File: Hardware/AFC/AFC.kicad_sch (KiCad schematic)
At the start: 80 parts, among them J1 Barrel_Jack_Switch, J2 Conn_Coaxial, J3 Conn_Coaxial, J4 Conn_Coaxial, J5 Conn_Coaxial, J6 Conn_Coaxial, J7 Conn_Coaxial, U1 AD633JRZ, U2 AD633JRZ, U3 AD630ARZ, U4 AD8429, U5 AD8429, U6 LM358, U7 LM358, U8 LM358

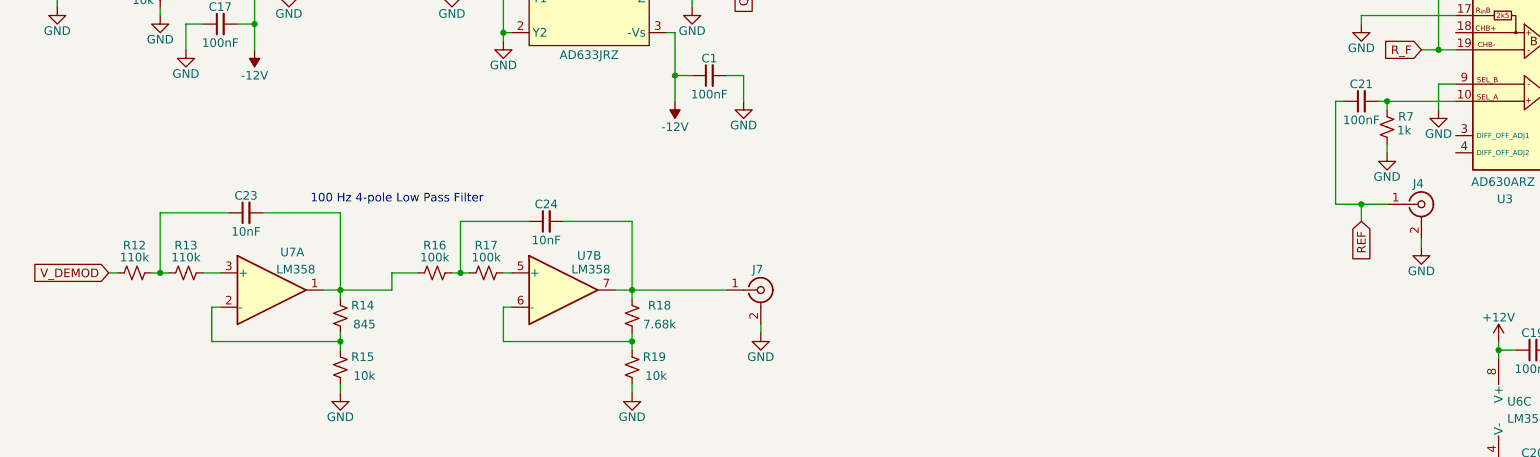
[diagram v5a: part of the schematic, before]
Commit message: Updating resistor values in filter
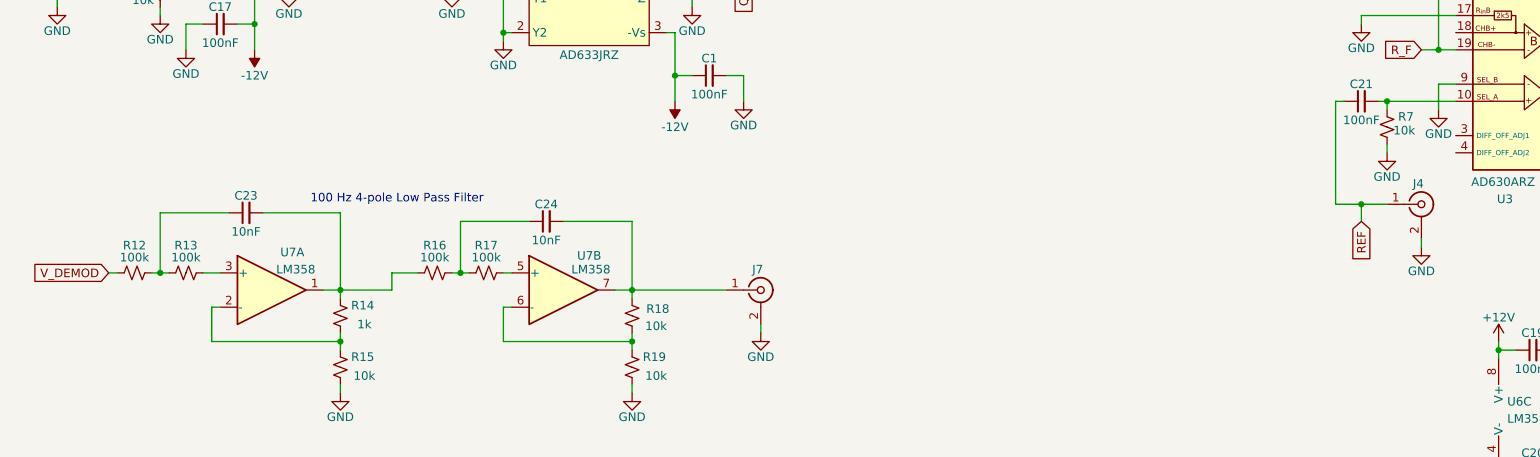
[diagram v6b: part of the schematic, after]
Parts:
- R12, R13: value 110k -> 100k
- R14: value 845 -> 1k
- R18: value 7.68k -> 10k
- R7: value 1k -> 10k
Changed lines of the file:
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@@
 			)
 		)
-		(property "Value" "110k"
+		(property "Value" "100k"
 			(at 34.29 125.984 90)
 			(effects
@@
 			)
 		)
-		(property "Value" "110k"
+		(property "Value" "100k"
 			(at 41.91 125.984 90)
 			(effects
@@
 		(dnp no)
 		(property "Reference" "R18"
-			(at 112.014 133.096 0)
+			(at 111.76 133.604 0)
 			(effects
 				(font
@@
 			)
 		)
-		(property "Value" "7.68k"
-			(at 112.014 135.89 0)
+		(property "Value" "10k"
+			(at 111.506 136.144 0)
 			(effects
 				(font
@@
 			)
 		)
-		(property "Value" "845"
+		(property "Value" "1k"
 			(at 68.326 135.89 0)
 			(effects
@@
 			)
 		)
-		(property "Value" "1k"
+		(property "Value" "10k"
 			(at 222.25 107.188 0)
 			(effects

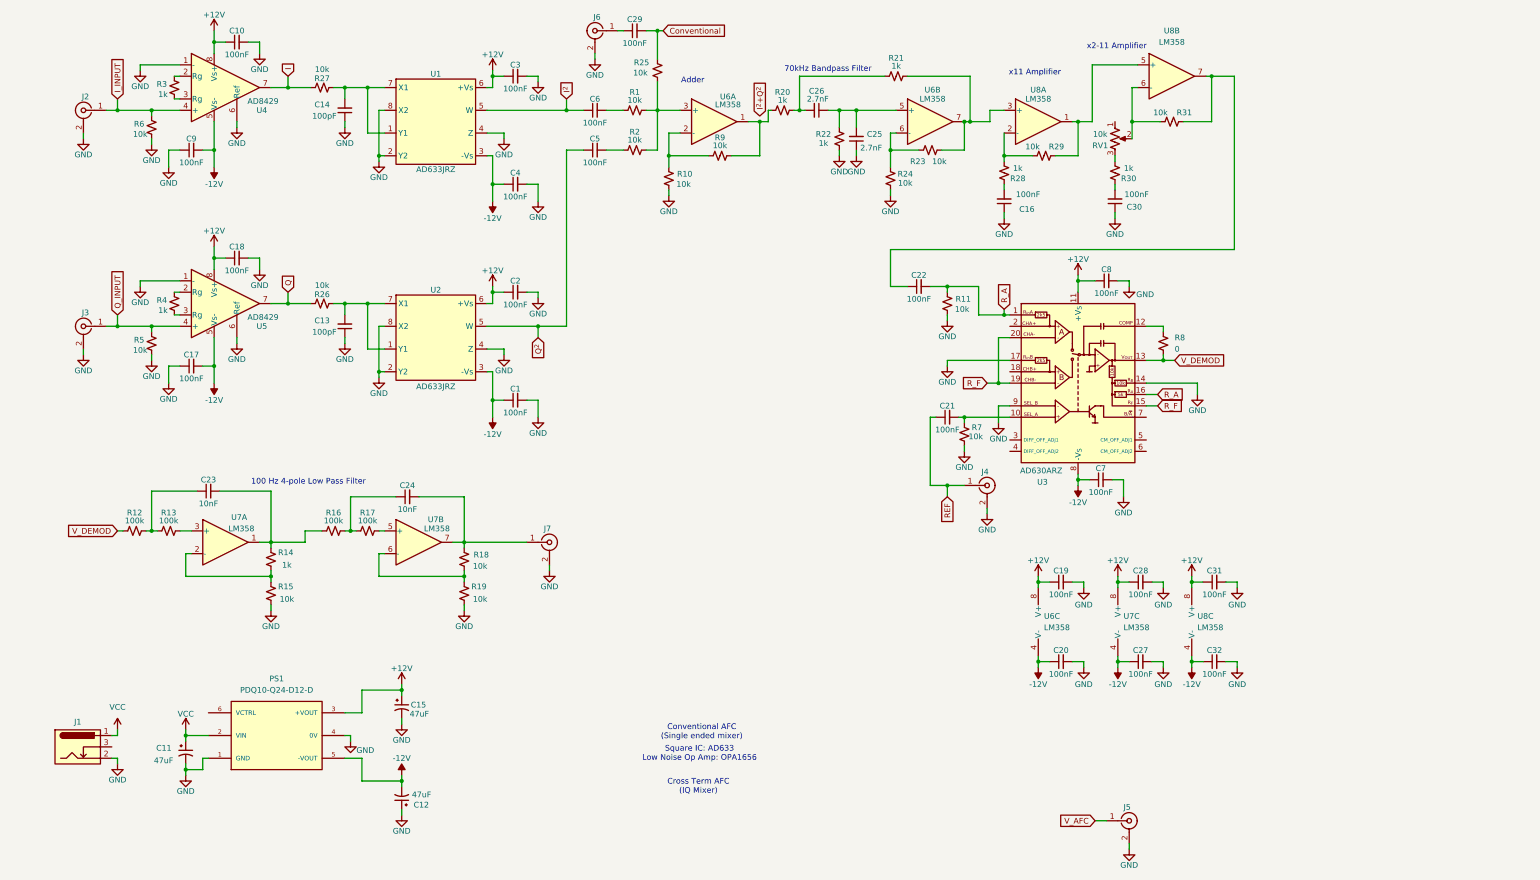
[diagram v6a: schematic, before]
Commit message: Adding amplifier
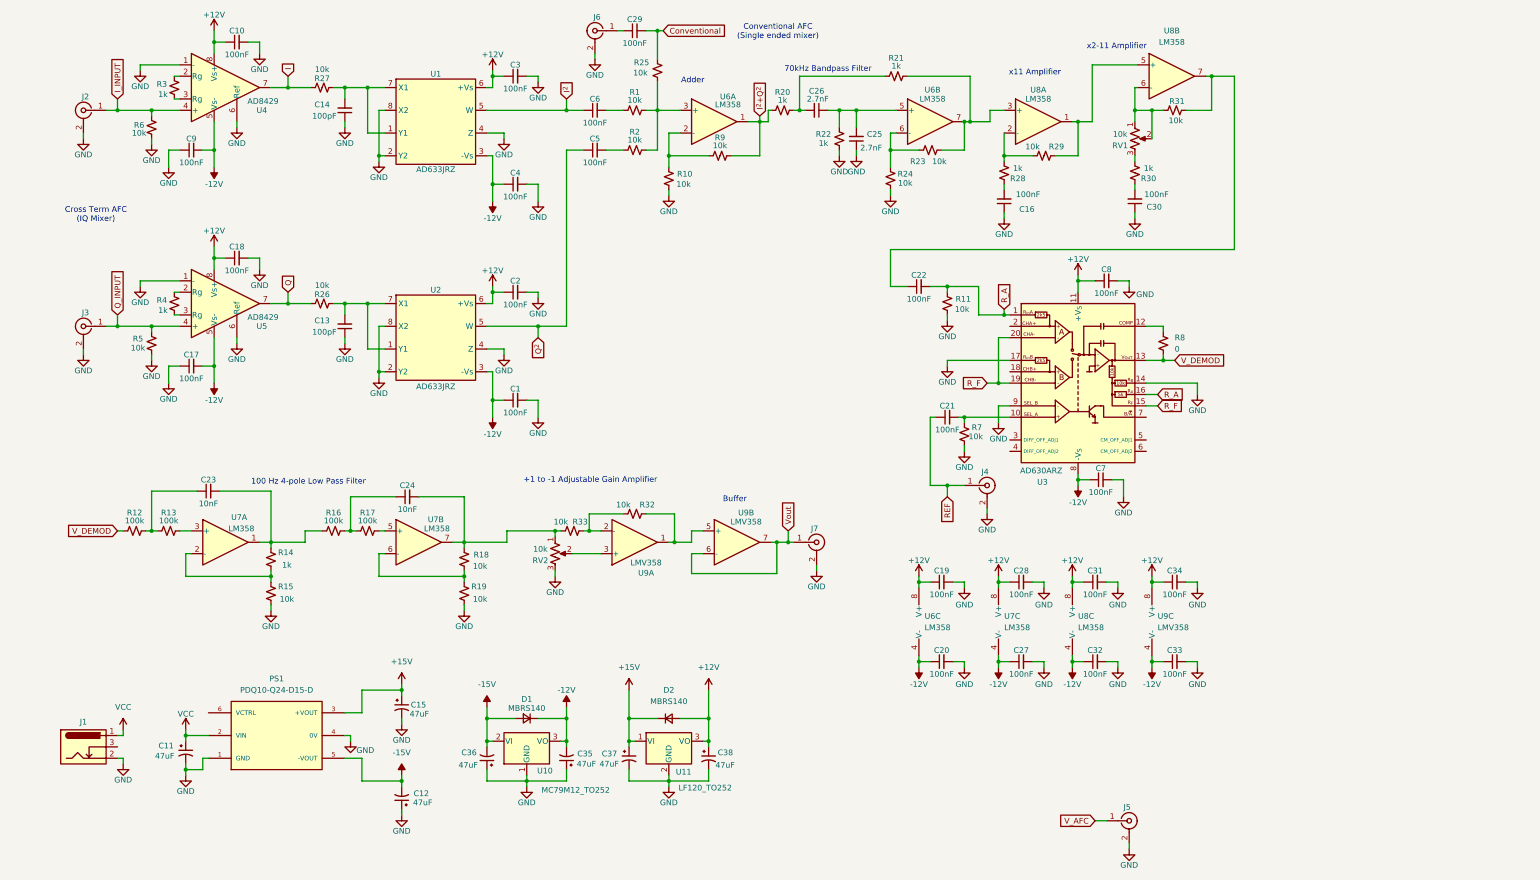
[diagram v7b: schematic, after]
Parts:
- added C33, C34: 100nF, symbol Device:C_Small
- added C35, C36, C37, C38: 47uF, symbol Device:C_Polarized_Small_US
- added D1, D2: MBRS140, symbol Device:D_Small
- added R32, R33: 10k, symbol Device:R_Small_US
- added RV2: 10k, symbol Device:R_Potentiometer_US
- added U10: MC79M12_TO252, Package_TO_SOT_SMD:TO-252-2, symbol Regulator_Linear:MC79M12_TO252
- added U11: LF120_TO252, Package_TO_SOT_SMD:TO-252-2, symbol Regulator_Linear:LF120_TO252
- added U9: LMV358, symbol Amplifier_Operational:LMV358
- PS1: value PDQ10-Q24-D12-D -> PDQ10-Q24-D15-D
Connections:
- net +12V: now also C34.1, C38.1, D2.2 (A), U11.3 (VO), U9.8 (V+); no longer C15.1, PS1.3 (+VOUT)
- net -12V: now also C33.1, C35.2, D1.1 (K), U10.3 (VO), U9.4 (V-); no longer C12.2, PS1.5 (-VOUT)
- net GND: now also C33.2, C34.2, C35.1, C36.1, C37.2, C38.2, RV2.3, U10.1 (GND), U11.2 (GND)
- net I^{2}+Q^{2}: now also R20.1, R9.2, U6.1
- net at C24.2, R18.2, U7.7: now also R33.1, RV2.1; no longer J7.1 (In)
- net at RV1.1: now also R31.1, RV1.2, U8.6 (-)
- new net: R32.1, R33.2, U9.2 (-)
- new net: R32.2, U9.1, U9.5 (+)
- new net: RV2.2, U9.3 (+)
- new net +15V: C15.1, C37.1, D2.1 (K), PS1.3 (+VOUT), U11.1 (VI)
- new net -15V: C12.2, C36.2, D1.2 (A), PS1.5 (-VOUT), U10.2 (VI)
- new net Vout: J7.1 (In), U9.6 (-), U9.7
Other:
- note added: "+1 to -1 Adjustable Gain Amplifier"
- note added: "Buffer"
- note removed: "Square IC: AD633 Low Noise Op Amp: OPA1656"
- moved on the sheet: C19, C20, C27, C28, C30, C31, C32, J1, J7, R30, R31, RV1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

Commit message: Adding low noise instrumentation amplifier to conventional AFC input
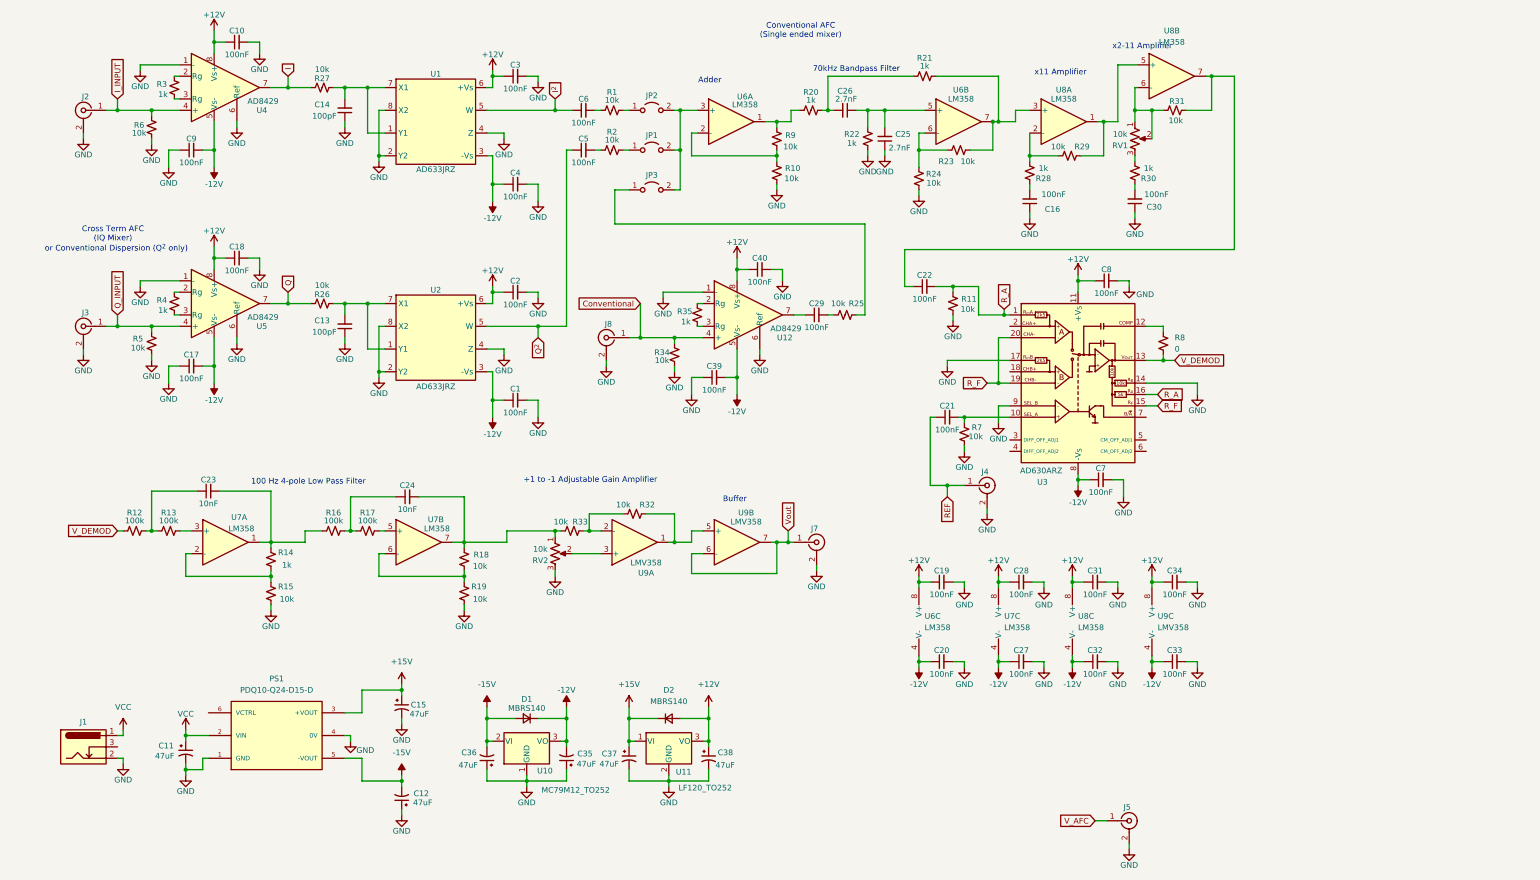
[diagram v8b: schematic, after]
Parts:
- removed J6: Conn_Coaxial, symbol Connector:Conn_Coaxial
- added C39, C40: 100nF, symbol Device:C_Small
- added J8: Conn_Coaxial, symbol Connector:Conn_Coaxial
- added JP1, JP2, JP3: Jumper_2_Open, symbol Jumper:Jumper_2_Open
- added R34: 10k, symbol Device:R_Small_US
- added R35: 1k, symbol Device:R_Small_US
- added U12: AD8429, symbol Amplifier_Instrumentation:AD8429
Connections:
- net +12V: now also C40.1, U12.8 (Vs+)
- net -12V: now also C39.2, U12.5 (Vs-)
- net Conventional: now also J8.1 (In), R34.2, U12.4 (+); no longer C29.2, R25.1
- net GND: now also C39.1, C40.2, J8.2 (Ext), R34.1, U12.1 (-), U12.6 (Ref)
- net at C29.1: now also U12.7
- net I^{2}+Q^{2}: no longer names the net of R20.1, R9.2, U6.1
- new net: JP3.1 (A), R25.1
- new net: JP1.2 (B), JP2.2 (B), JP3.2 (B), U6.3 (+)
- new net: JP2.1 (A), R1.2
- new net: R35.1, U12.3 (Rg)
- new net: R35.2, U12.2 (Rg)
- new net: C29.2, R25.2
- new net: JP1.1 (A), R2.2
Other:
- note added: "or Conventional Dispersion (Q^{2} only)"
- moved on the sheet: C16, C22, C25, C26, C29, C5, C6, R1, R10, R11, R2, R20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
